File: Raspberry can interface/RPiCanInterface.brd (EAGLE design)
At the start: 100 x 80 mm, 16 parts, among them IC1 MCP2515-E/P

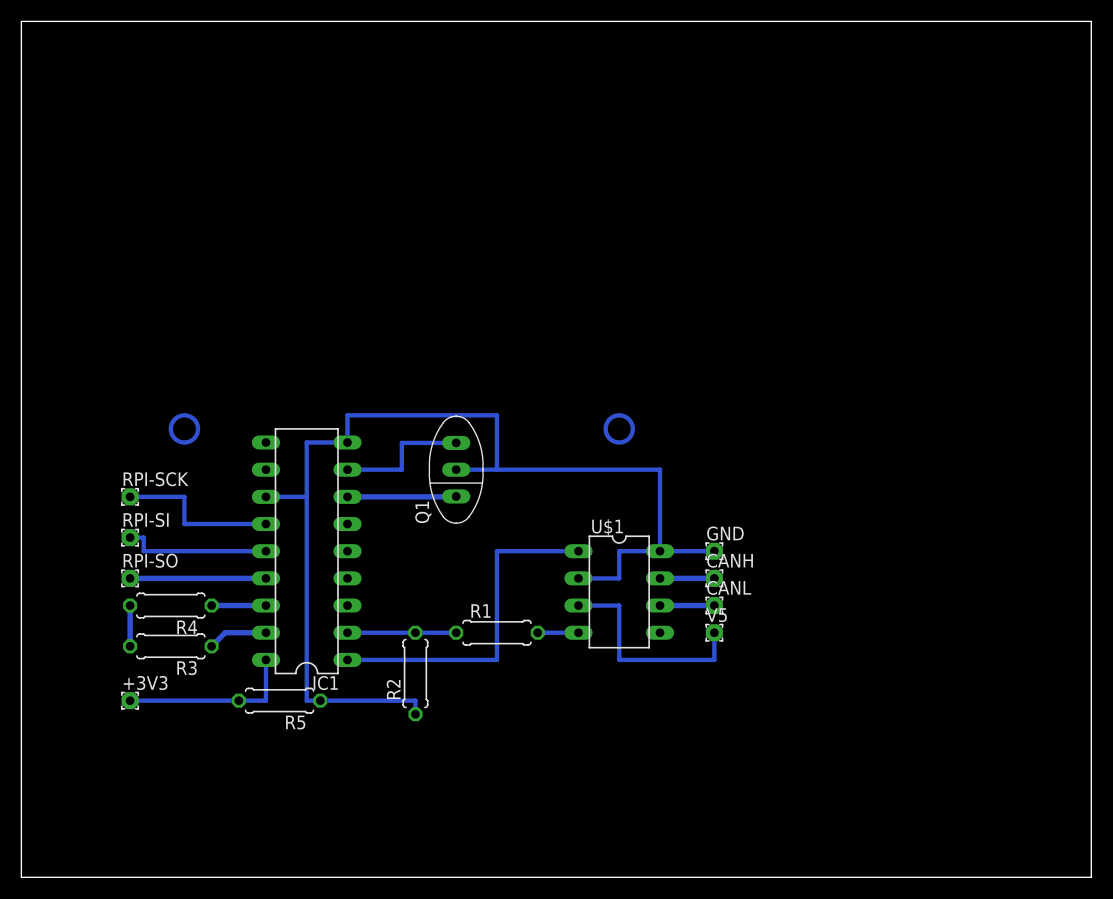
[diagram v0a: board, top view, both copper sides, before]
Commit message: updated pi can board
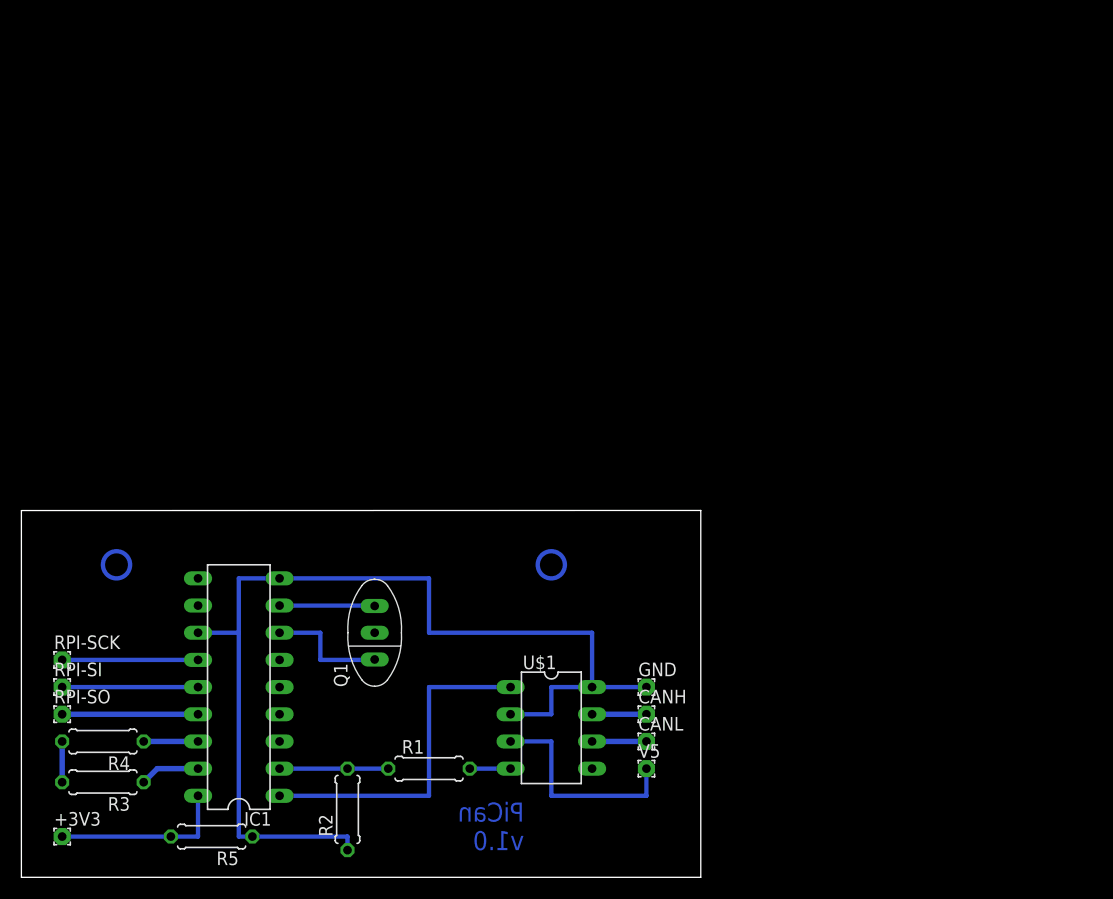
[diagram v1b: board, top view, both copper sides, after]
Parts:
- moved Q1 17.0 mm to (33.0, 22.9)
- moved RPI-SCK 16.5 mm to (3.81, 20.3)
- moved RPI-SI 15.3 mm to (3.81, 17.8)
- moved +3V3 14.2 mm to (3.81, 3.81)
- moved RPI-SO 14.2 mm to (3.81, 15.2)
- moved U$1 14.2 mm to (49.5, 14.0)
- moved CANH 14.2 mm to (58.4, 15.2)
- moved IC1 14.2 mm to (20.3, 17.8)
- moved R1 14.2 mm to (38.1, 10.2)
- moved R2 14.2 mm to (30.5, 6.35)
- moved R3 14.2 mm to (7.62, 8.89)
- moved R4 14.2 mm to (7.62, 12.7)
- moved R5 14.2 mm to (17.8, 3.81)
- moved CANL 14.2 mm to (58.4, 12.7)
- moved GND 14.2 mm to (58.4, 17.8)
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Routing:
- net GND: track 106.7 -> 97.8 mm
- net N$5: track 12.7 -> 8.93 mm
- net N$12: track 15.2 -> 12.7 mm
- net N$4: track 10.2 -> 11.5 mm
- net N$11: track 14.0 -> 12.7 mm
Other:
- board size 100 x 80 mm -> 63.5 x 34.3 mm
- board text added: "PiCan v1.0"
